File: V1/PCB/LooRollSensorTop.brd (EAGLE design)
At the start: 25 x 100 mm, 18 parts, among them Q1 200mA/50V, U1 HTU21DSMD

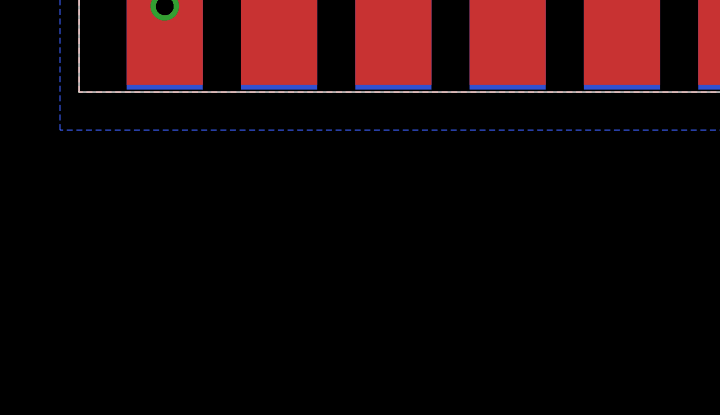
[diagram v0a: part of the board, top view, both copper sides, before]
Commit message: Added bodge resistor required to pull LED drive low to prevent LEDs switching on when Photon is in power save mode.
"Printed" eagle files as pdfs.
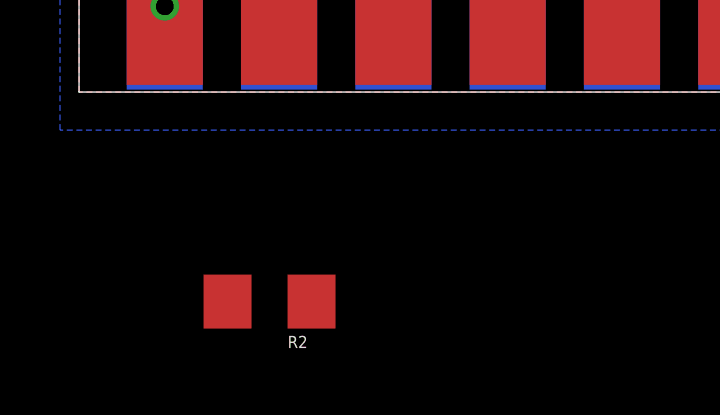
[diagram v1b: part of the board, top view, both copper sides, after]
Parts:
- added R2: 100k, SparkFun-Resistors:1206
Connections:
- net GND: now also R2.2
- net LEDDRIVE: now also R2.1
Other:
- board text added: "Bodge Resistor - hand fit."
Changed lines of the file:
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@@
 <text x="22.86" y="6.0325" size="0.8128" layer="26" rot="MR0">R4</text>
 <text x="7.62" y="6.0325" size="0.8128" layer="26" rot="MR0">3v3</text>
+<text x="41.275" y="-6.0325" size="1.778" layer="48" rot="R180">Bodge Resistor - hand fit.</text>
 </plain>
 <attributes>
@@
 <attribute name="NAME" x="9.2075" y="37.6555" size="0.8128" layer="25"/>
 </element>
+<element name="R2" library="SparkFun-Resistors" package="1206" value="100k" x="6.35" y="-6.985" rot="R180"/>
 </elements>
 <signals>
@@
 <via x="24.13" y="98.95" extent="1-16" drill="0.6"/>
 <via x="0.9525" y="98.95" extent="1-16" drill="0.6"/>
+<contactref element="R2" pad="2"/>
+<wire x1="10.5825" y1="92.71" x2="24.13" y2="98.95" width="0" layer="19" extent="1-1"/>
+<wire x1="9.525" y1="92.71" x2="10.5825" y2="92.71" width="0" layer="19" extent="1-1"/>
+<wire x1="10.7775" y1="88.6475" x2="10.5825" y2="92.71" width="0" layer="19" extent="1-16"/>
+<wire x1="12.2775" y1="88.6475" x2="10.7775" y2="88.6475" width="0" layer="19" extent="16-16"/>
+<wire x1="16.9625" y1="83.5975" x2="12.2775" y2="88.6475" width="0" layer="19" extent="16-16"/>
+<wire x1="12.455" y1="81.65" x2="16.9625" y2="83.5975" width="0" layer="19" extent="16-16"/>
+<wire x1="0.9525" y1="98.95" x2="9.525" y2="92.71" width="0" layer="19" extent="1-1"/>
+<wire x1="3.54" y1="75.3395" x2="12.455" y2="81.65" width="0" layer="19" extent="16-16"/>
+<wire x1="21.32" y1="70.2595" x2="16.9625" y2="83.5975" width="0" layer="19" extent="16-16"/>
+<wire x1="14.3095" y1="42.28" x2="21.32" y2="70.2595" width="0" layer="19" extent="1-1"/>
+<wire x1="13.6525" y1="39.26" x2="14.3095" y2="42.28" width="0" layer="19" extent="1-1"/>
+<wire x1="17.145" y1="33.545" x2="13.6525" y2="39.26" width="0" layer="19" extent="1-1"/>
+<wire x1="6.6675" y1="39.26" x2="13.6525" y2="39.26" width="0" layer="19" extent="1-1"/>
+<wire x1="4.08" y1="43.1825" x2="6.6675" y2="39.26" width="0" layer="19" extent="1-1"/>
+<wire x1="2.8575" y1="2.8575" x2="17.145" y2="33.545" width="0" layer="19" extent="1-1"/>
+<wire x1="2.8575" y1="2.7775" x2="2.8575" y2="2.8575" width="0" layer="19" extent="1-1"/>
+<wire x1="2.8575" y1="2.62" x2="2.8575" y2="2.7775" width="0" layer="19" extent="1-16"/>
+<wire x1="4.95" y1="-6.985" x2="2.8575" y2="2.62" width="0" layer="19" extent="1-16"/>
 </signal>
 <signal name="VBAT">
@@
 <wire x1="4.3975" y1="45.7675" x2="1.3175" y2="45.7675" width="0.4064" layer="16"/>
 <wire x1="1.3175" y1="45.7675" x2="1.27" y2="45.72" width="0.4064" layer="16"/>
+<contactref element="R2" pad="1"/>
+<wire x1="10.4775" y1="2.7775" x2="7.75" y2="-6.985" width="0" layer="19" extent="1-1"/>
 </signal>
 <signal name="WATERSENSE">
